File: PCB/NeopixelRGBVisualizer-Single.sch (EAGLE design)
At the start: 19 parts, among them IC1 MSGEQ7, Q1 16MHz, X1 STEREOJACK, X2 1751251

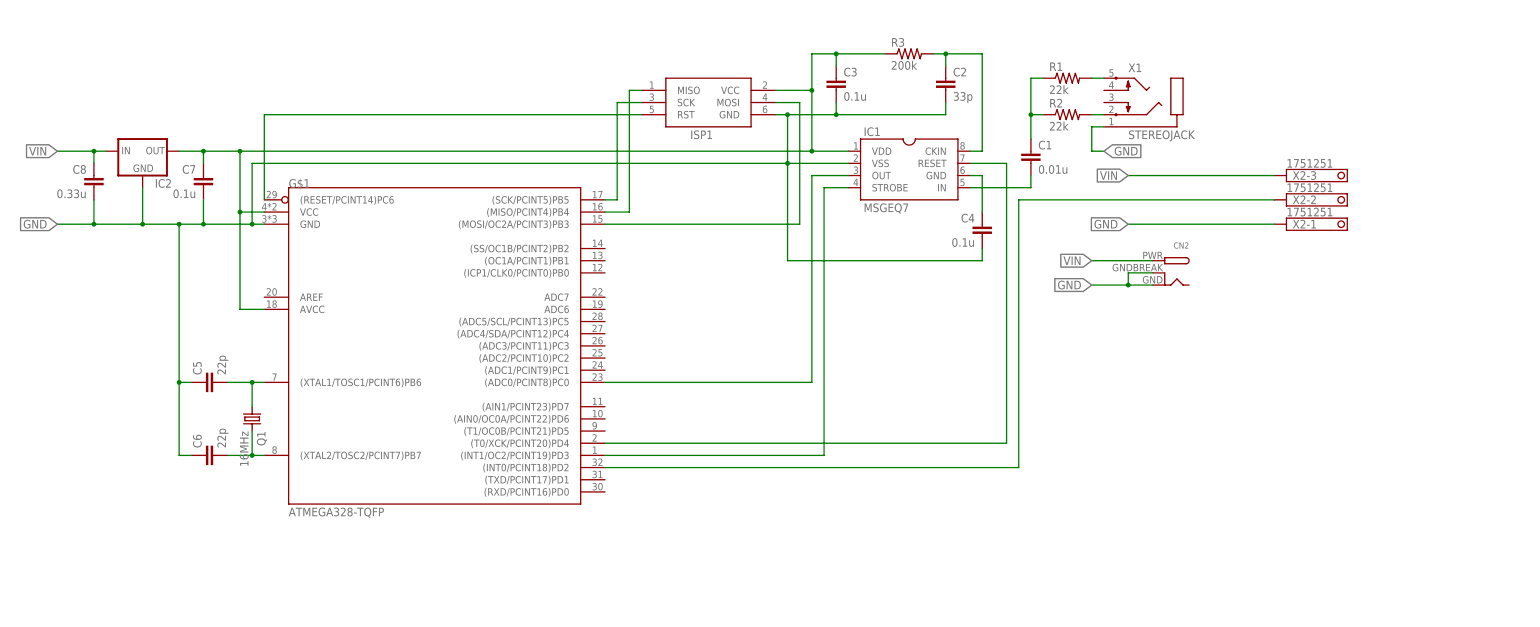
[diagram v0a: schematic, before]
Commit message: Almost ready for second prototype order -Added 3 tactile buttons for control inputs: "Power","+","-" -Changed Phoenix screw terminal to Molex Mini-Fit Jr receptacle -Added small potentiometer as input volume control -Aligned receptacles with board edge
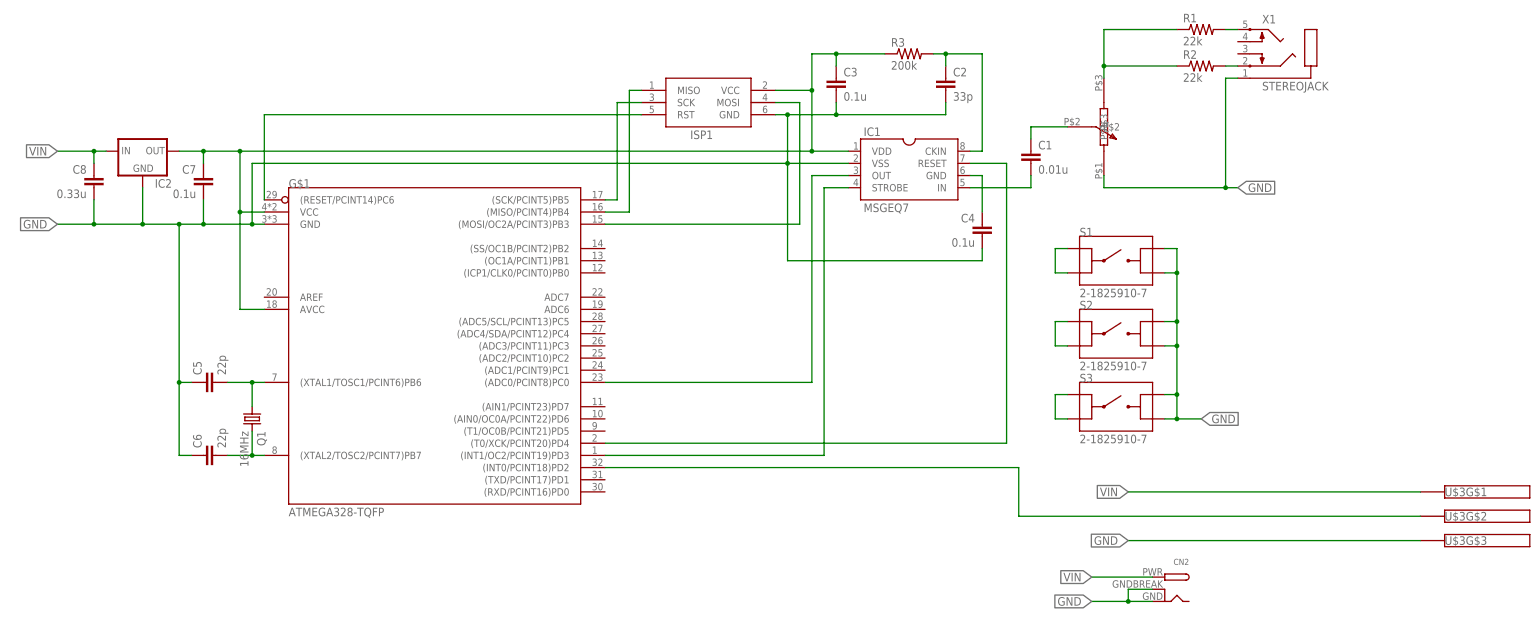
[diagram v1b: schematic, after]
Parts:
- removed X2: 1751251, con-phoenix-350:1751251
- added S1, S2, S3: 2-1825910-7, 2-1825910-7:2-1825910-7
- added U$2: PTD901-2015K, potentiometers:PTD901-2015K
- added U$3: 0039303035, MinifitJR:0039303035
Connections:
- new net N$16: C1.1, U$2.P$2
- new net N$18: S1.1, S1.2
- new net N$19: S2.1, S2.2
- new net N$20: S3.1, S3.2
- net GND: now also S1.3, S1.4, S2.3, S2.4, S3.3, S3.4, U$2.P$1, U$3G$3.P$1; no longer X2-1.K
- net N$17: now also U$3G$2.P$1; no longer X2-2.K
- net N$6: now also U$2.P$3; no longer C1.1
- net VIN: now also U$3G$1.P$1; no longer X2-3.K
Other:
- moved on the sheet: CN2, R1, R2, X1

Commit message: Reverted to first prototype, designing second prototype using updated libraries.
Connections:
- net N$18: now also U$1.(AIN1/PCINT23)PD7
- net N$19: now also U$1.(AIN0/OC0A/PCINT22)PD6
- net N$20: now also U$1.(T1/OC0B/PCINT21)PD5
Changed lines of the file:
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@@
 <pinref part="S1" gate="G$1" pin="1"/>
 <wire x1="170.18" y1="58.42" x2="167.64" y2="58.42" width="0.1524" layer="91"/>
-<wire x1="167.64" y1="58.42" x2="167.64" y2="53.34" width="0.1524" layer="91"/>
+<wire x1="167.64" y1="58.42" x2="167.64" y2="55.88" width="0.1524" layer="91"/>
 <pinref part="S1" gate="G$1" pin="2"/>
+<wire x1="167.64" y1="55.88" x2="167.64" y2="53.34" width="0.1524" layer="91"/>
 <wire x1="167.64" y1="53.34" x2="170.18" y2="53.34" width="0.1524" layer="91"/>
+<pinref part="U$1" gate="G$1" pin="(AIN1/PCINT23)PD7"/>
+<wire x1="73.66" y1="25.4" x2="160.02" y2="25.4" width="0.1524" layer="91"/>
+<wire x1="160.02" y1="25.4" x2="160.02" y2="55.88" width="0.1524" layer="91"/>
+<wire x1="160.02" y1="55.88" x2="167.64" y2="55.88" width="0.1524" layer="91"/>
+<junction x="167.64" y="55.88"/>
 </segment>
 </net>
@@
 <pinref part="S2" gate="G$1" pin="1"/>
 <wire x1="170.18" y1="43.18" x2="167.64" y2="43.18" width="0.1524" layer="91"/>
-<wire x1="167.64" y1="43.18" x2="167.64" y2="38.1" width="0.1524" layer="91"/>
+<wire x1="167.64" y1="43.18" x2="167.64" y2="40.64" width="0.1524" layer="91"/>
 <pinref part="S2" gate="G$1" pin="2"/>
+<wire x1="167.64" y1="40.64" x2="167.64" y2="38.1" width="0.1524" layer="91"/>
 <wire x1="167.64" y1="38.1" x2="170.18" y2="38.1" width="0.1524" layer="91"/>
+<wire x1="167.64" y1="40.64" x2="162.56" y2="40.64" width="0.1524" layer="91"/>
+<wire x1="162.56" y1="40.64" x2="162.56" y2="22.86" width="0.1524" layer="91"/>
+<junction x="167.64" y="40.64"/>
+<pinref part="U$1" gate="G$1" pin="(AIN0/OC0A/PCINT22)PD6"/>
+<wire x1="162.56" y1="22.86" x2="73.66" y2="22.86" width="0.1524" layer="91"/>
 </segment>
 </net>
@@
 <wire x1="170.18" y1="27.94" x2="167.64" y2="27.94" width="0.1524" layer="91"/>
 <pinref part="S3" gate="G$1" pin="2"/>
-<wire x1="167.64" y1="27.94" x2="167.64" y2="22.86" width="0.1524" layer="91"/>
+<wire x1="167.64" y1="27.94" x2="167.64" y2="25.4" width="0.1524" layer="91"/>
+<wire x1="167.64" y1="25.4" x2="167.64" y2="22.86" width="0.1524" layer="91"/>
 <wire x1="167.64" y1="22.86" x2="170.18" y2="22.86" width="0.1524" layer="91"/>
+<pinref part="U$1" gate="G$1" pin="(T1/OC0B/PCINT21)PD5"/>
+<wire x1="73.66" y1="20.32" x2="165.1" y2="20.32" width="0.1524" layer="91"/>
+<wire x1="165.1" y1="20.32" x2="165.1" y2="25.4" width="0.1524" layer="91"/>
+<wire x1="165.1" y1="25.4" x2="167.64" y2="25.4" width="0.1524" layer="91"/>
+<junction x="167.64" y="25.4"/>
 </segment>
 </net>

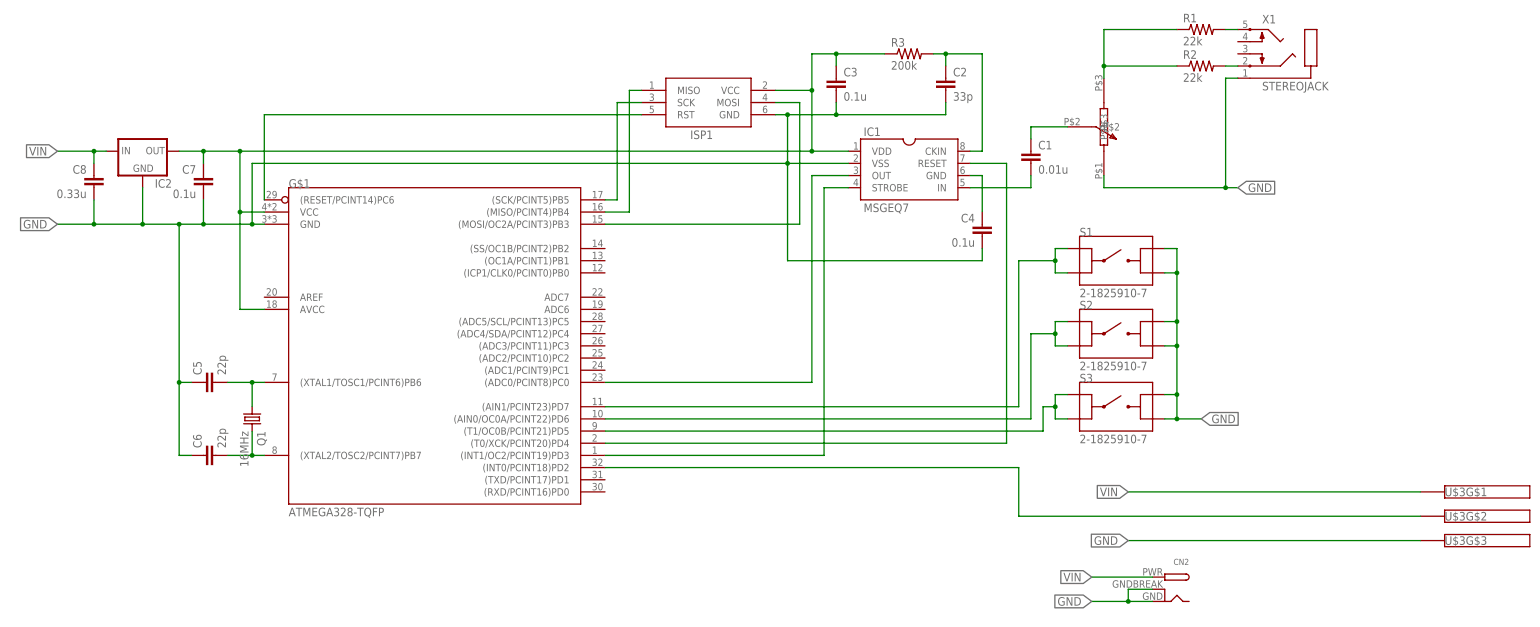
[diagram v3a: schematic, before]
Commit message: Very tight design, needs to be fit into a larger enclosure.
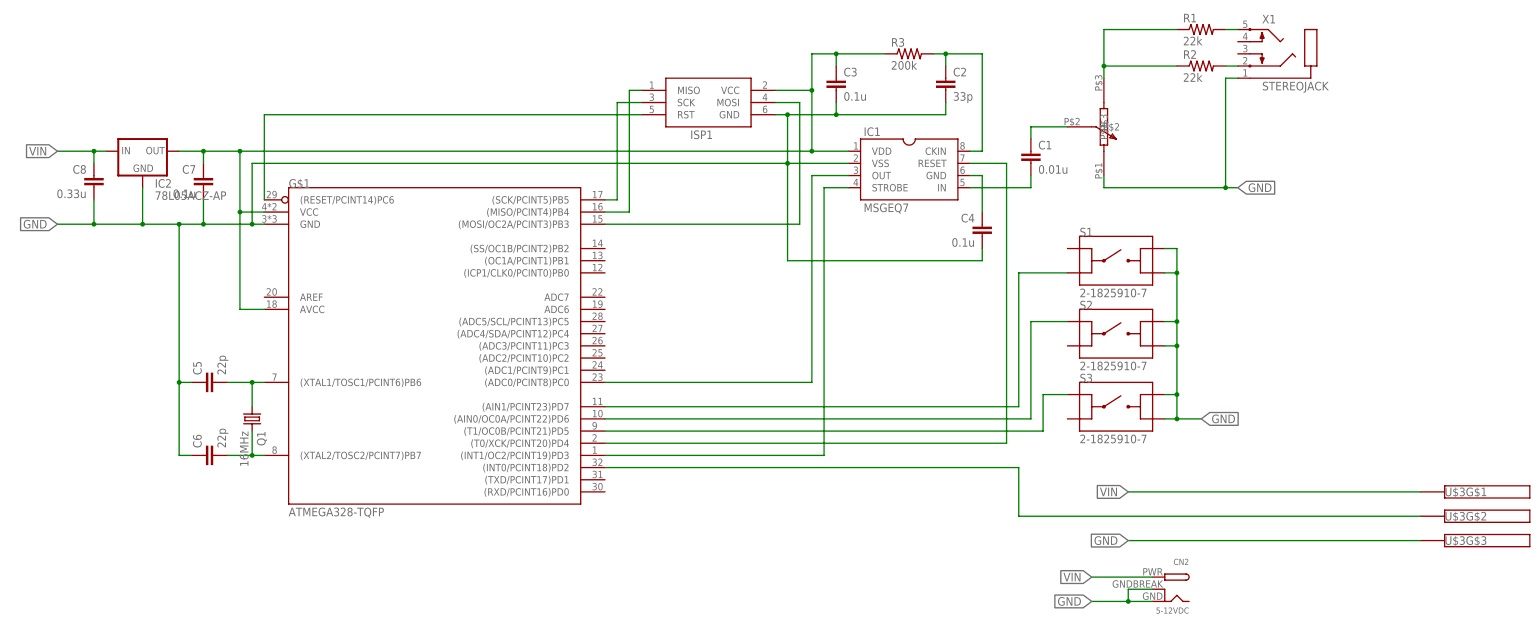
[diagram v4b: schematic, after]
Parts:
- CN2: value (none) -> 5-12VDC
- IC2: value (none) -> 78L05ACZ-AP
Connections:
- net N$18: no longer S1.1
- net N$19: no longer S2.2
- net N$20: no longer S3.2
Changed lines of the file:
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@@
 <part name="C5" library="rcl" deviceset="C-EU" device="C0805" value="22p"/>
 <part name="C6" library="rcl" deviceset="C-EU" device="C0805" value="22p"/>
-<part name="CN2" library="adafruit" deviceset="DCBARREL" device="PTH"/>
+<part name="CN2" library="adafruit" deviceset="DCBARREL" device="PTH" value="5-12VDC"/>
 <part name="C7" library="rcl" deviceset="C-EU" device="C0805" value="0.1u"/>
 <part name="C8" library="rcl" deviceset="C-EU" device="C0805" value="0.33u"/>
-<part name="IC2" library="v-reg" deviceset="78LXX" device=""/>
+<part name="IC2" library="v-reg" deviceset="78LXX" device="" value="78L05ACZ-AP"/>
 <part name="U$2" library="potentiometers" deviceset="PTD901-2015K" device=""/>
 <part name="S1" library="2-1825910-7" deviceset="2-1825910-7" device=""/>
@@
 </segment>
 <segment>
-<pinref part="CN2" gate="G$1" pin="GNDBREAK"/>
 <pinref part="CN2" gate="G$1" pin="GND"/>
 <wire x1="187.96" y1="-15.24" x2="182.88" y2="-15.24" width="0.1524" layer="91"/>
+<label x="175.26" y="-15.24" size="1.778" layer="95" rot="R180" xref="yes"/>
+<pinref part="CN2" gate="G$1" pin="GNDBREAK"/>
 <wire x1="182.88" y1="-15.24" x2="175.26" y2="-15.24" width="0.1524" layer="91"/>
 <wire x1="187.96" y1="-12.7" x2="182.88" y2="-12.7" width="0.1524" layer="91"/>
 <wire x1="182.88" y1="-12.7" x2="182.88" y2="-15.24" width="0.1524" layer="91"/>
 <junction x="182.88" y="-15.24"/>
-<label x="175.26" y="-15.24" size="1.778" layer="95" rot="R180" xref="yes"/>
 </segment>
 <segment>
@@
 <net name="N$18" class="0">
 <segment>
-<pinref part="S1" gate="G$1" pin="1"/>
-<wire x1="170.18" y1="58.42" x2="167.64" y2="58.42" width="0.1524" layer="91"/>
-<wire x1="167.64" y1="58.42" x2="167.64" y2="55.88" width="0.1524" layer="91"/>
 <pinref part="S1" gate="G$1" pin="2"/>
-<wire x1="167.64" y1="55.88" x2="167.64" y2="53.34" width="0.1524" layer="91"/>
-<wire x1="167.64" y1="53.34" x2="170.18" y2="53.34" width="0.1524" layer="91"/>
 <pinref part="U$1" gate="G$1" pin="(AIN1/PCINT23)PD7"/>
 <wire x1="73.66" y1="25.4" x2="160.02" y2="25.4" width="0.1524" layer="91"/>
-<wire x1="160.02" y1="25.4" x2="160.02" y2="55.88" width="0.1524" layer="91"/>
-<wire x1="160.02" y1="55.88" x2="167.64" y2="55.88" width="0.1524" layer="91"/>
-<junction x="167.64" y="55.88"/>
+<wire x1="160.02" y1="25.4" x2="160.02" y2="53.34" width="0.1524" layer="91"/>
+<wire x1="160.02" y1="53.34" x2="170.18" y2="53.34" width="0.1524" layer="91"/>
 </segment>
 </net>
@@
 <segment>
 <pinref part="S2" gate="G$1" pin="1"/>
-<wire x1="170.18" y1="43.18" x2="167.64" y2="43.18" width="0.1524" layer="91"/>
-<wire x1="167.64" y1="43.18" x2="167.64" y2="40.64" width="0.1524" layer="91"/>
-<pinref part="S2" gate="G$1" pin="2"/>
-<wire x1="167.64" y1="40.64" x2="167.64" y2="38.1" width="0.1524" layer="91"/>
-<wire x1="167.64" y1="38.1" x2="170.18" y2="38.1" width="0.1524" layer="91"/>
-<wire x1="167.64" y1="40.64" x2="162.56" y2="40.64" width="0.1524" layer="91"/>
-<wire x1="162.56" y1="40.64" x2="162.56" y2="22.86" width="0.1524" layer="91"/>
-<junction x="167.64" y="40.64"/>
+<wire x1="170.18" y1="43.18" x2="162.56" y2="43.18" width="0.1524" layer="91"/>
+<wire x1="162.56" y1="43.18" x2="162.56" y2="22.86" width="0.1524" layer="91"/>
 <pinref part="U$1" gate="G$1" pin="(AIN0/OC0A/PCINT22)PD6"/>
 <wire x1="162.56" y1="22.86" x2="73.66" y2="22.86" width="0.1524" layer="91"/>
@@
 <segment>
 <pinref part="S3" gate="G$1" pin="1"/>
-<wire x1="170.18" y1="27.94" x2="167.64" y2="27.94" width="0.1524" layer="91"/>
-<pinref part="S3" gate="G$1" pin="2"/>
-<wire x1="167.64" y1="27.94" x2="167.64" y2="25.4" width="0.1524" layer="91"/>
-<wire x1="167.64" y1="25.4" x2="167.64" y2="22.86" width="0.1524" layer="91"/>
-<wire x1="167.64" y1="22.86" x2="170.18" y2="22.86" width="0.1524" layer="91"/>
 <pinref part="U$1" gate="G$1" pin="(T1/OC0B/PCINT21)PD5"/>
 <wire x1="73.66" y1="20.32" x2="165.1" y2="20.32" width="0.1524" layer="91"/>
-<wire x1="165.1" y1="20.32" x2="165.1" y2="25.4" width="0.1524" layer="91"/>
-<wire x1="165.1" y1="25.4" x2="167.64" y2="25.4" width="0.1524" layer="91"/>
-<junction x="167.64" y="25.4"/>
+<wire x1="165.1" y1="20.32" x2="165.1" y2="27.94" width="0.1524" layer="91"/>
+<wire x1="165.1" y1="27.94" x2="170.18" y2="27.94" width="0.1524" layer="91"/>
 </segment>
 </net>
@@
 </sheet>
 </sheets>
-<errors>
-</errors>
 </schematic>
 </drawing>

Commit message: Prototype version 2 with buttons and Molex minifit jr connector with shape appropriate for project boxes
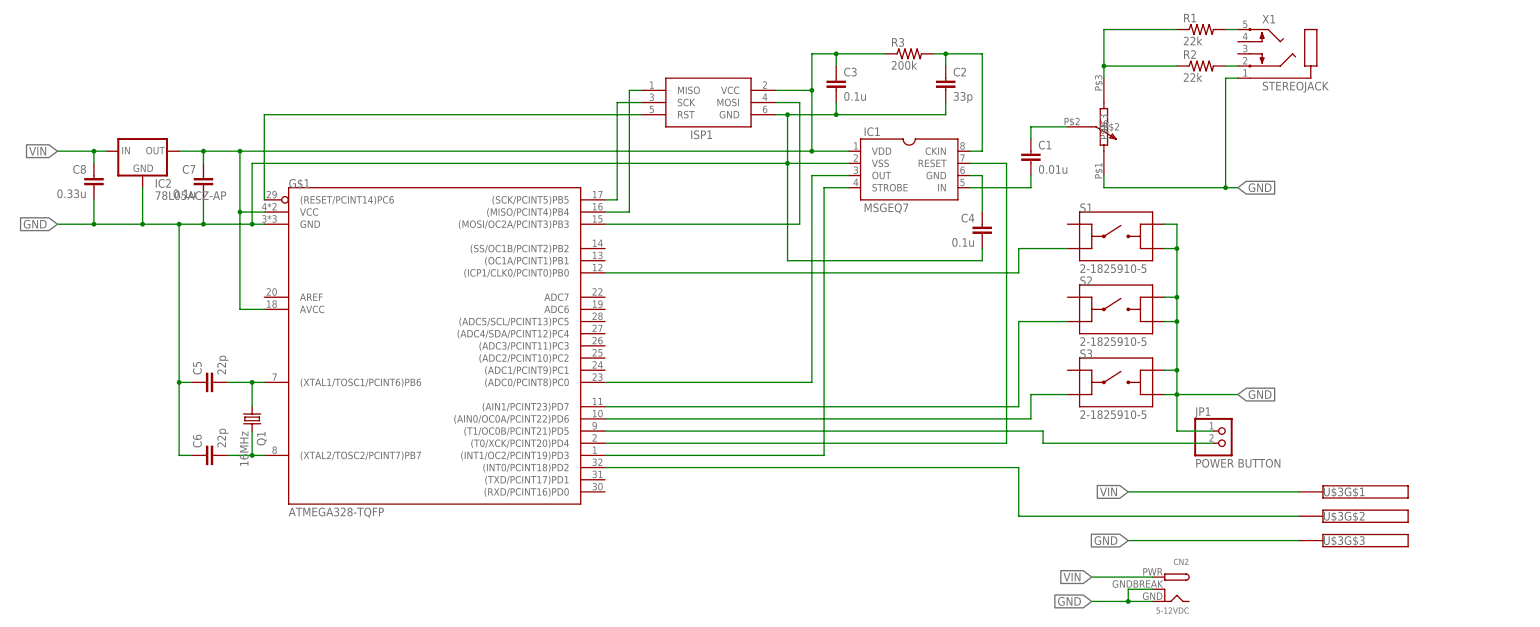
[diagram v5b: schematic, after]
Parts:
- added JP1: POWER BUTTON, mypinhead:PINHD-1X2/ROUND
- S1, S2, S3: value 2-1825910-7 -> 2-1825910-5; device 2-1825910-7:2-1825910-7 -> te_tactileswitch:2-1825910-5
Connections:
- net N$7 renamed MSGEQ7_OUT
- net N$8 renamed MSGEQ7_STROBE
- net N$9 renamed MSGEQ7_RESET
- new net N$8: S2.2, U$1.(AIN1/PCINT23)PD7
- net GND: now also JP1.1
- net N$18: now also U$1.(ICP1/CLK0/PCINT0)PB0; no longer U$1.(AIN1/PCINT23)PD7
- net N$19: now also S3.2; no longer S2.1
- net N$20: now also JP1.2; no longer S3.1
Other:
- moved on the sheet: S1, S2, S3, U$3G$1, U$3G$2, U$3G$3

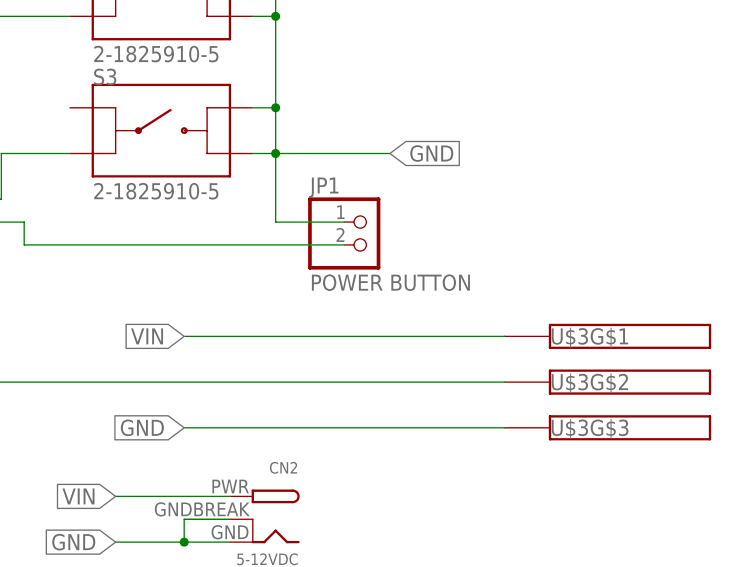
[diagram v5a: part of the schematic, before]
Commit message: Partially completed silkscreen for v2 production
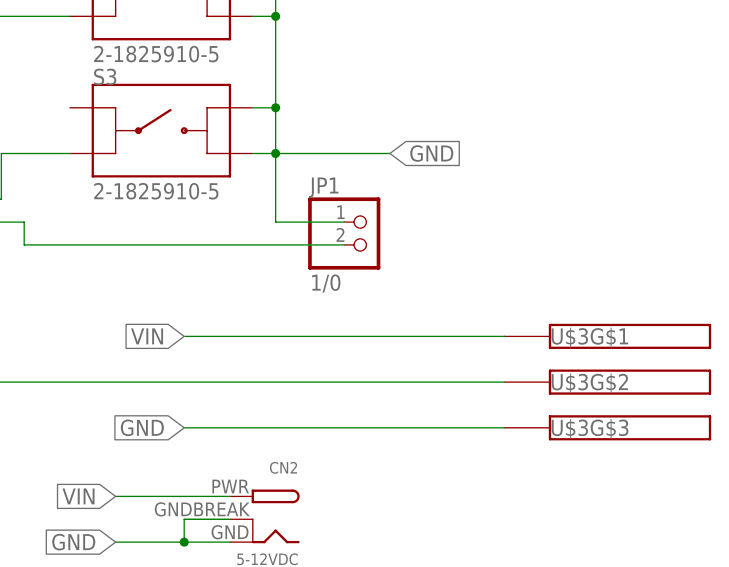
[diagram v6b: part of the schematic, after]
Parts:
- JP1: value POWER BUTTON -> 1/0
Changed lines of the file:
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@@
 <part name="S3" library="te_tactileswitch" deviceset="2-1825910-5" device=""/>
 <part name="U$3" library="MinifitJR" deviceset="0039303035" device=""/>
-<part name="JP1" library="mypinhead" deviceset="PINHD-1X2" device="/ROUND" value="POWER BUTTON"/>
+<part name="JP1" library="mypinhead" deviceset="PINHD-1X2" device="/ROUND" value="1/0"/>
 </parts>
 <sheets>
